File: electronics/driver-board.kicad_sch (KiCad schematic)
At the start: 61 parts, among them J1 Conn_01x01_Socket, J10 USB_C_Receptacle_USB2.0, J2 Conn_01x03_Pin, J3 Conn_01x06, J4 Qwiic_RA, J6 Conn_01x03_Pin, J8 Conn_01x04_Pin, J9 Conn_01x01_Socket, SW1 SW_Push, SW2 SW_Push, SW3 SW_Push, SW4 SW_Push, U1 LMR16006YQ3, U3 ESP32-C6-MINI-1/U, U5 TMC5240-TSSOP38, U7 AS5047D

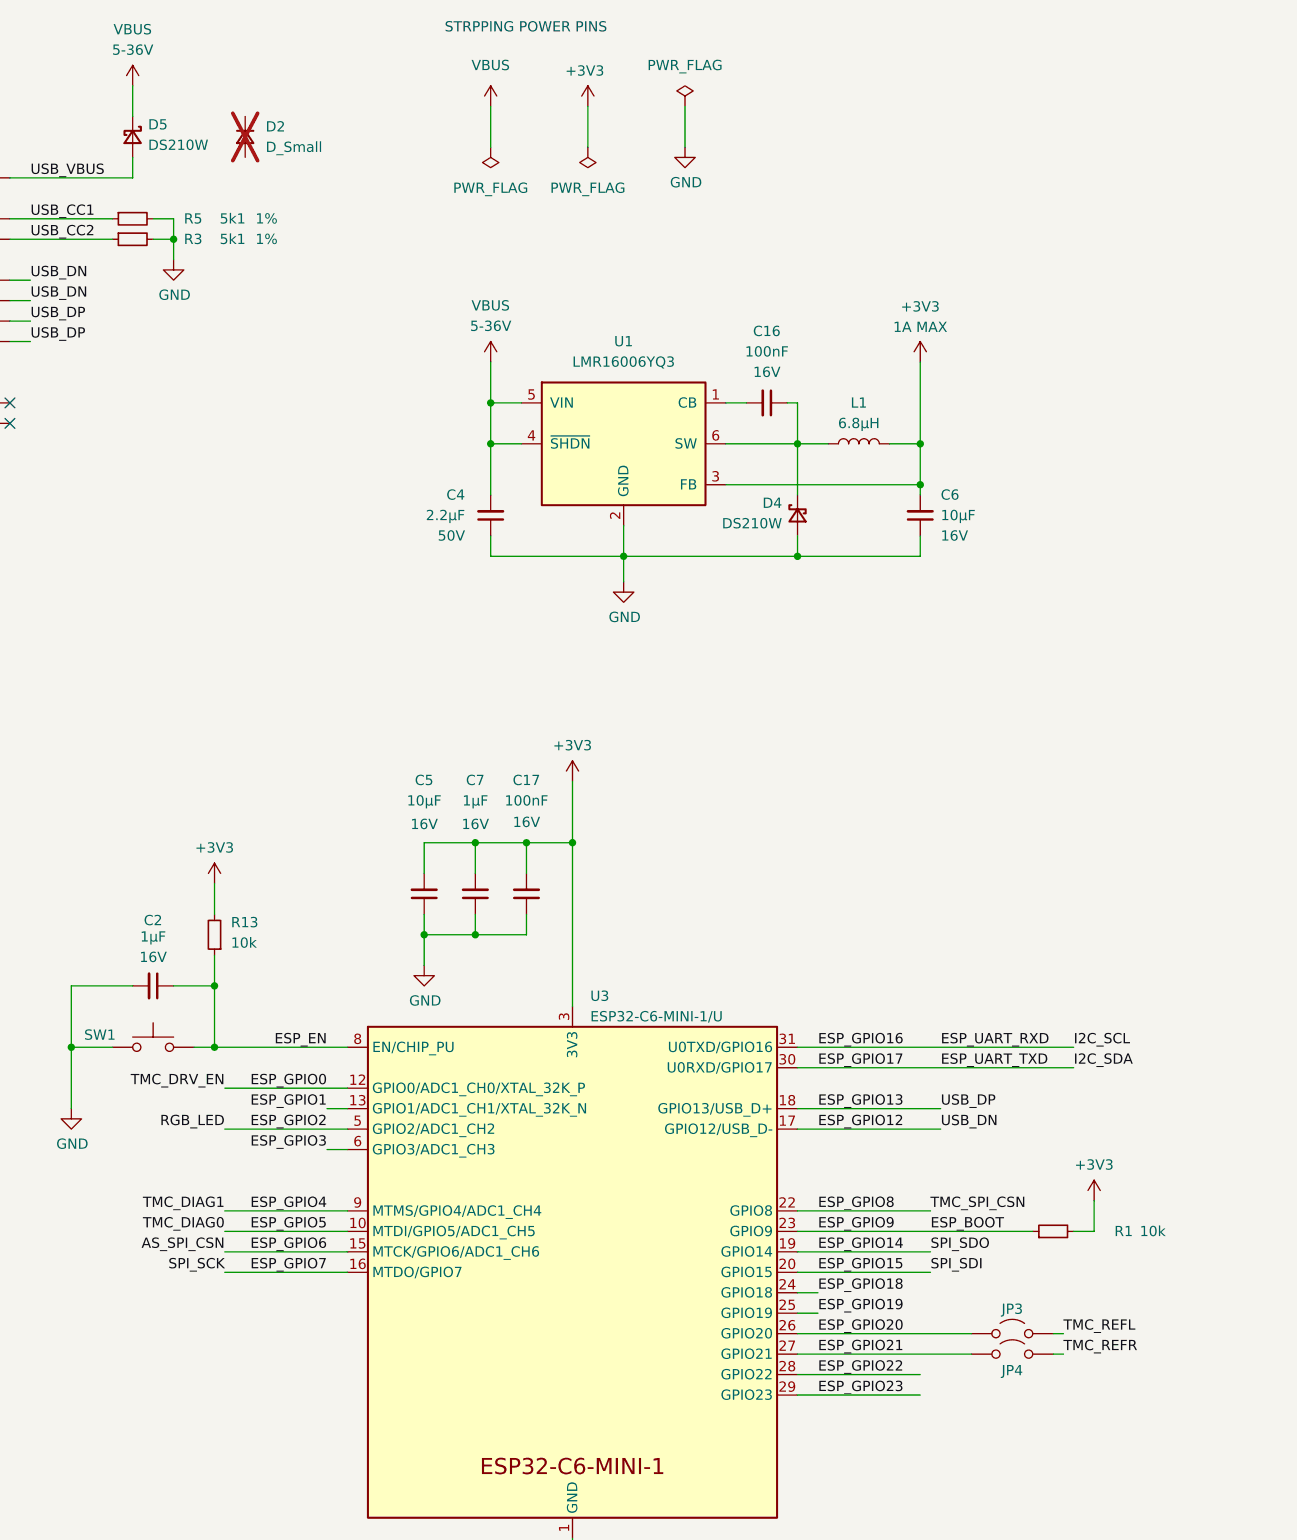
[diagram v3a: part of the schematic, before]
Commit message: wip 4-layer layout
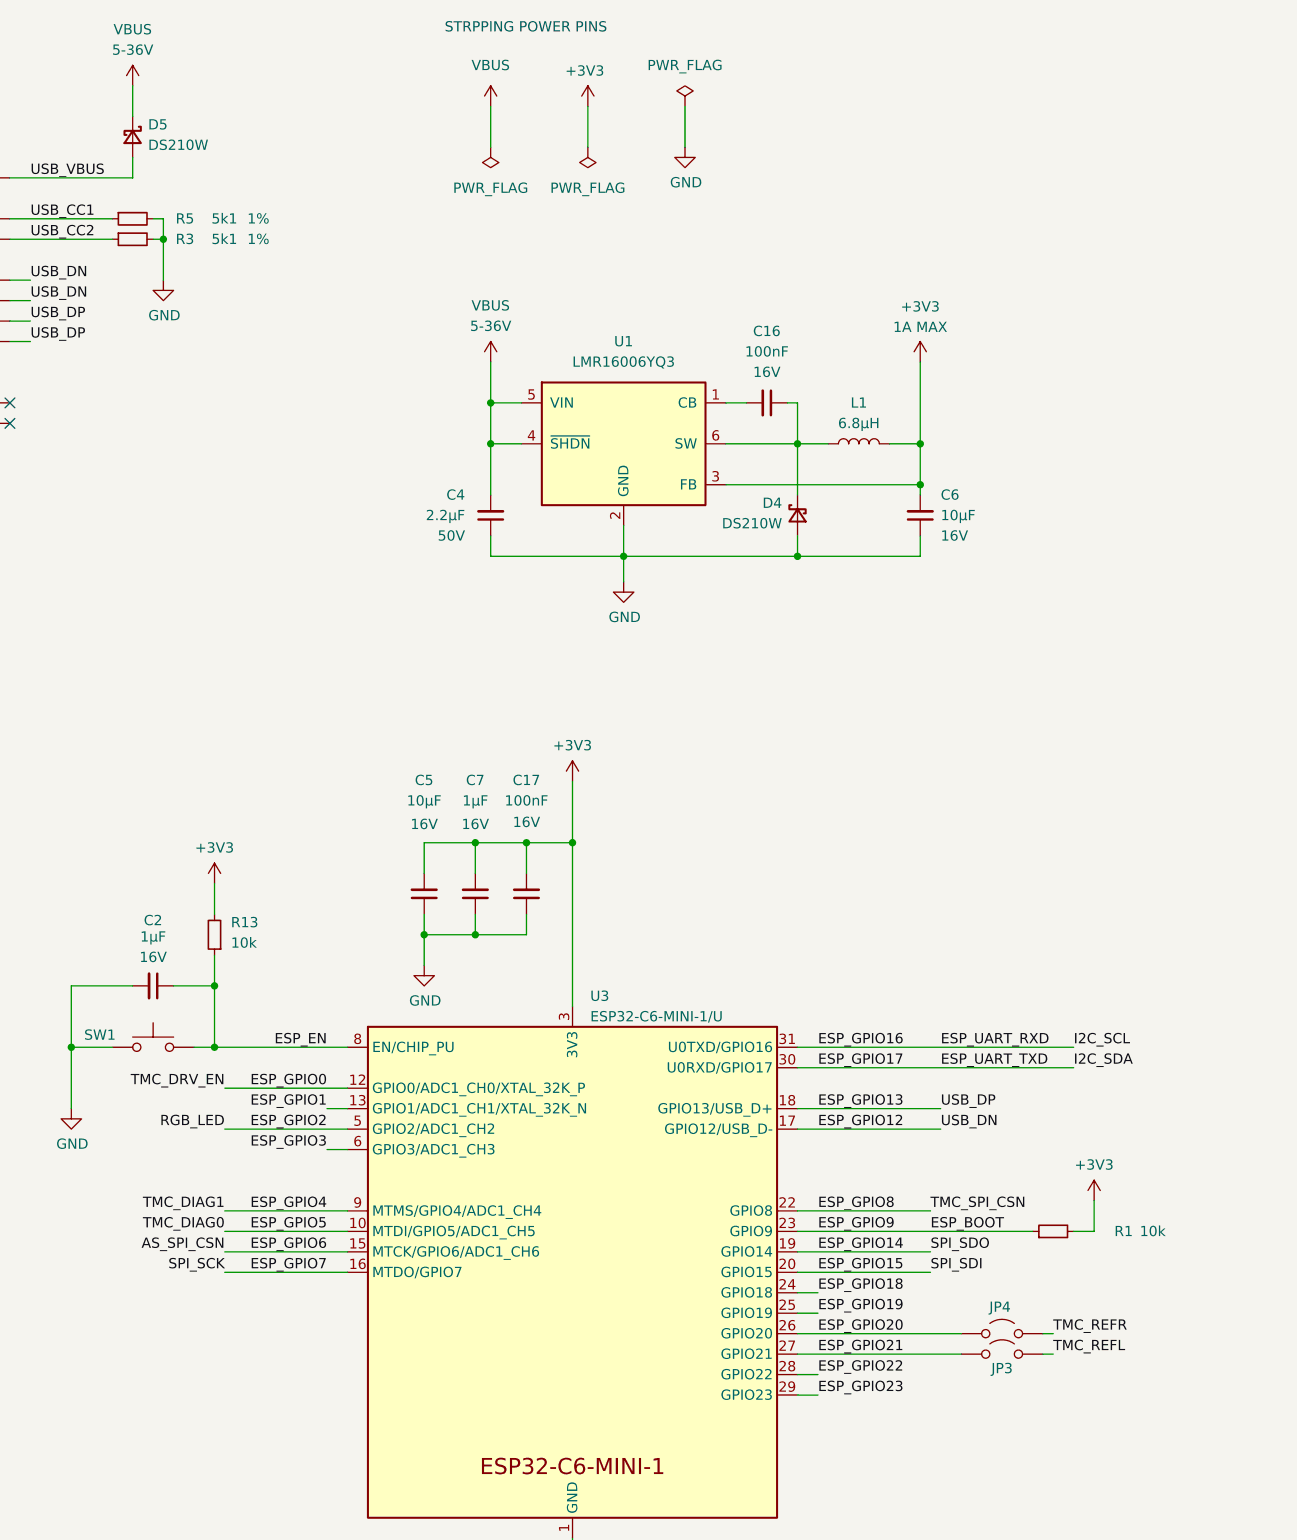
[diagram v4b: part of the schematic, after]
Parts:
- removed D2: D_Small, symbol Device:D_Small
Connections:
- net ESP_GPIO20: now also JP4.2 (B); no longer JP3.1 (A)
- net ESP_GPIO21: now also JP3.1 (A); no longer JP4.2 (B)
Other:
- moved on the sheet: JP3, JP4
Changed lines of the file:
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@@
 	)
 	(junction
-		(at 72.39 45.72)
+		(at 71.12 45.72)
 		(diameter 0)
 		(color 0 0 0 0)
@@
 	(wire
 		(pts
-			(xy 72.39 43.18) (xy 69.85 43.18)
+			(xy 71.12 43.18) (xy 69.85 43.18)
 		)
 		(stroke
@@
 	(wire
 		(pts
-			(xy 149.86 186.69) (xy 165.1 186.69)
+			(xy 149.86 186.69) (xy 152.4 186.69)
 		)
 		(stroke
@@
 	(wire
 		(pts
-			(xy 182.88 181.61) (xy 181.61 181.61)
+			(xy 181.61 184.15) (xy 180.34 184.15)
 		)
 		(stroke
@@
 	(wire
 		(pts
-			(xy 149.86 184.15) (xy 171.45 184.15)
+			(xy 149.86 184.15) (xy 170.18 184.15)
 		)
 		(stroke
@@
 	(wire
 		(pts
-			(xy 69.85 45.72) (xy 72.39 45.72)
+			(xy 69.85 45.72) (xy 71.12 45.72)
 		)
 		(stroke
@@
 	(wire
 		(pts
-			(xy 72.39 43.18) (xy 72.39 45.72)
+			(xy 71.12 43.18) (xy 71.12 45.72)
 		)
 		(stroke
@@
 	(wire
 		(pts
-			(xy 149.86 181.61) (xy 171.45 181.61)
+			(xy 149.86 181.61) (xy 170.18 181.61)
 		)
 		(stroke
@@
 	(wire
 		(pts
-			(xy 181.61 184.15) (xy 182.88 184.15)
+			(xy 180.34 181.61) (xy 181.61 181.61)
 		)
 		(stroke
@@
 	(wire
 		(pts
-			(xy 149.86 189.23) (xy 165.1 189.23)
+			(xy 149.86 189.23) (xy 152.4 189.23)
 		)
 		(stroke
@@
 	(wire
 		(pts
-			(xy 72.39 45.72) (xy 72.39 48.26)
+			(xy 71.12 45.72) (xy 71.12 50.8)
 		)
 		(stroke
@@
 	)
 	(label "TMC_REFL"
-		(at 182.88 181.61 0)
+		(at 181.61 184.15 0)
 		(fields_autoplaced yes)
 		(effects
@@
 	)
 	(label "TMC_REFR"
-		(at 182.88 184.15 0)
+		(at 181.61 181.61 0)
 		(fields_autoplaced yes)
 		(effects
@@
 		(dnp no)
 		(property "Reference" "R3"
-			(at 73.66 45.72 90)
+			(at 72.644 45.72 90)
 			(effects
 				(font
@@
 		)
 		(property "Value" "5k1"
-			(at 78.105 45.72 90)
+			(at 77.089 45.72 90)
 			(effects
 				(font
@@
 		)
 		(property "Tolerance" "1%"
-			(at 82.55 45.72 90)
+			(at 81.534 45.72 90)
 			(effects
 				(font
@@
 	(symbol
 		(lib_id "power:GND")
-		(at 72.39 48.26 0)
+		(at 71.12 50.8 0)
 		(unit 1)
 		(exclude_from_sim no)
@@
 		(dnp no)
 		(property "Reference" "#PWR042"
-			(at 72.39 54.61 0)
+			(at 71.12 57.15 0)
 			(effects
 				(font
@@
 		)
 		(property "Value" "GND"
-			(at 72.517 52.6542 0)
+			(at 71.247 55.1942 0)
 			(effects
 				(font
@@
 		)
 		(property "Footprint" ""
-			(at 72.39 48.26 0)
+			(at 71.12 50.8 0)
 			(effects
 				(font
@@
 		)
 		(property "Datasheet" ""
-			(at 72.39 48.26 0)
+			(at 71.12 50.8 0)
 			(effects
 				(font
@@
 		)
 		(property "Description" ""
-			(at 72.39 48.26 0)
+			(at 71.12 50.8 0)
 			(effects
 				(font
@@
 	(symbol
 		(lib_id "Jumper:Jumper_2_Open")
-		(at 176.53 181.61 0)
+		(at 175.26 184.15 0)
 		(unit 1)
 		(exclude_from_sim yes)
@@
 		(dnp no)
 		(property "Reference" "JP3"
-			(at 176.53 178.562 0)
+			(at 175.26 185.928 0)
 			(effects
 				(font
@@
 		)
 		(property "Value" "Jumper_2_Open"
-			(at 176.53 177.8 0)
+			(at 175.26 180.34 0)
 			(effects
 				(font
@@
 		)
 		(property "Footprint" "Jumper:SolderJumper-2_P1.3mm_Open_Pad1.0x1.5mm"
-			(at 176.53 181.61 0)
+			(at 175.26 184.15 0)
 			(effects
 				(font
@@
 		)
 		(property "Datasheet" "~"
-			(at 176.53 181.61 0)
+			(at 175.26 184.15 0)
 			(effects
 				(font
@@
 		)
 		(property "Description" "Jumper, 2-pole, open"
-			(at 176.53 181.61 0)
+			(at 175.26 184.15 0)
 			(effects
 				(font
@@
 	(symbol
 		(lib_id "Jumper:Jumper_2_Open")
-		(at 176.53 184.15 0)
+		(at 175.26 181.61 0)
 		(mirror y)
 		(unit 1)
@@
 		(dnp no)
 		(property "Reference" "JP4"
-			(at 176.53 186.182 0)
+			(at 175.006 178.308 0)
 			(effects
 				(font
@@
 		)
 		(property "Value" "Jumper_2_Open"
-			(at 176.53 180.34 0)
+			(at 175.26 177.8 0)
 			(effects
 				(font
@@
 		)
 		(property "Footprint" "Jumper:SolderJumper-2_P1.3mm_Open_Pad1.0x1.5mm"
-			(at 176.53 184.15 0)
+			(at 175.26 181.61 0)
 			(effects
 				(font
@@
 		)
 		(property "Datasheet" "~"
-			(at 176.53 184.15 0)
+			(at 175.26 181.61 0)
 			(effects
 				(font
@@
 		)
 		(property "Description" "Jumper, 2-pole, open"
-			(at 176.53 184.15 0)
+			(at 175.26 181.61 0)
 			(effects
 				(font
@@
 		(dnp no)
 		(property "Reference" "R5"
-			(at 73.66 43.18 90)
+			(at 72.644 43.18 90)
 			(effects
 				(font
@@
 		)
 		(property "Value" "5k1"
-			(at 78.105 43.18 90)
+			(at 77.089 43.18 90)
 			(effects
 				(font
@@
 		)
 		(property "Tolerance" "1%"
-			(at 82.55 43.18 90)
+			(at 81.534 43.18 90)
 			(effects
 				(font
@@
 					(unit 1)
 				)
-			)
-		)
-	)
-	(symbol
-		(lib_id "Device:D_Small")
-		(at 81.28 33.02 270)
-		(unit 1)
-		(exclude_from_sim no)
-		(in_bom no)
-		(on_board no)
-		(dnp yes)
-		(property "Reference" "D2"
-			(at 83.82 31.75 90)
-			(effects
-				(font
-					(size 1.27 1.27)
-				)
-				(justify left)
-			)
-		)
-		(property "Value" "D_Small"
-			(at 83.82 34.29 90)
-			(effects
-				(font
-					(size 1.27 1.27)
-				)
-				(justify left)
-			)
-		)
-		(property "Footprint" ""
-			(at 81.28 33.02 90)
-			(effects
-				(font
-					(size 1.27 1.27)
-				)
-				(hide yes)
-			)
-		)
-		(property "Datasheet" "~"
-			(at 81.28 33.02 90)
-			(effects
-				(font
-					(size 1.27 1.27)
-				)
-				(hide yes)
-			)
-		)
-		(property "Description" ""
-			(at 81.28 33.02 0)
-			(effects
-				(font
-					(size 1.27 1.27)
-				)
-				(hide yes)
-			)
-		)
-		(property "Sim.Device" "D"
-			(at 81.28 33.02 0)
-			(effects
-				(font
-					(size 1.27 1.27)
-				)
-				(hide yes)
-			)
-		)
-		(property "Sim.Pins" "1=K 2=A"
-			(at 81.28 33.02 0)
-			(effects
-				(font
-					(size 1.27 1.27)
-				)
-				(hide yes)
-			)
-		)
-		(pin "2"
-		)
-		(pin "1"
-		)
-		(instances
-			(project "driver-board"
-				(path "/597a11f2-5d2c-4a65-ac95-38ad106e1367"
-					(reference "D2")
-					(unit 1)
-				)

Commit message: more routing
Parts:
- removed J2, J6: Conn_01x03_Pin, Connector_PinHeader_2.54mm:PinHeader_1x03_P2.54mm_Vertical, symbol Connector:Conn_01x03_Pin
- removed J8: Conn_01x04_Pin, Connector_PinHeader_2.54mm:PinHeader_1x04_P2.54mm_Vertical, symbol Connector:Conn_01x04_Pin
- added J5: Conn_02x03_Counter_Clockwise, Connector_PinHeader_2.54mm:PinHeader_2x03_P2.54mm_Vertical, symbol Connector_Generic:Conn_02x03_Counter_Clockwise
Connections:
- net +3V3: now also J5.3 (Pin_3), J5.4 (Pin_4)
- net BTN2: now also U3.28 (GPIO22); no longer U3.29 (GPIO23)
- net BTN3: now also U3.29 (GPIO23); no longer U3.28 (GPIO22)
- net ESP_GPIO3: now also JP2.2 (B)
- net GND: now also J5.1 (Pin_1), J5.2 (Pin_2)
- net TMC_REFL: now also J5.6 (Pin_6)
- net TMC_REFR: now also J5.5 (Pin_5)
- net AS_CLK renamed ESP_GPIO7
- net AS_MISO renamed ESP_GPIO14
- net AS_MOSI renamed ESP_GPIO15
- net ESP_GPIO15: no longer JP2.2 (B)
- net AS_SPI_CSN renamed ESP_GPIO6
